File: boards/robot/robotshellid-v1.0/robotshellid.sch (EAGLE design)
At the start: 38 parts, among them IC1 PCA9848PWJ, U2 TSL25721FN, U3 TSL25721FN, U4 TSL25721FN, U5 TSL25721FN, U6 MIC5501-3.0YM5-TR

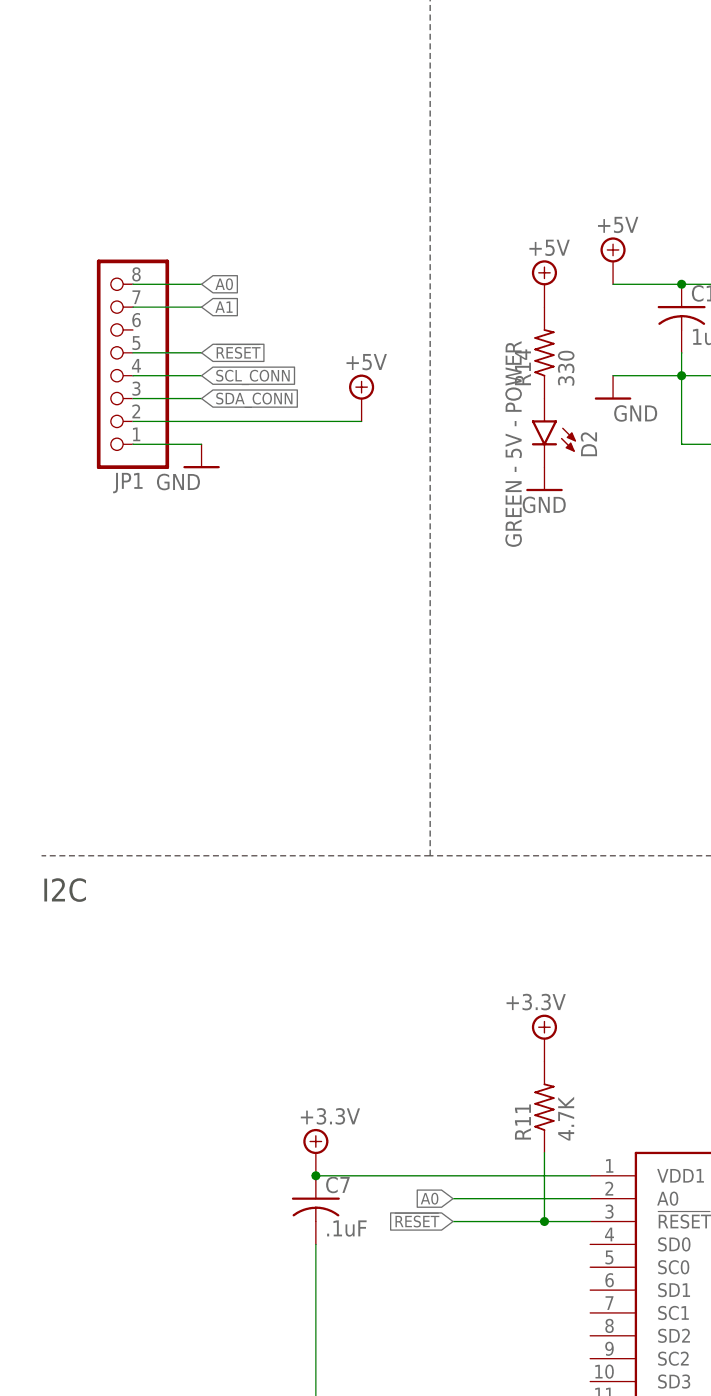
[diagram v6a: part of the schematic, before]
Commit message: Changed connector out for ffc connector
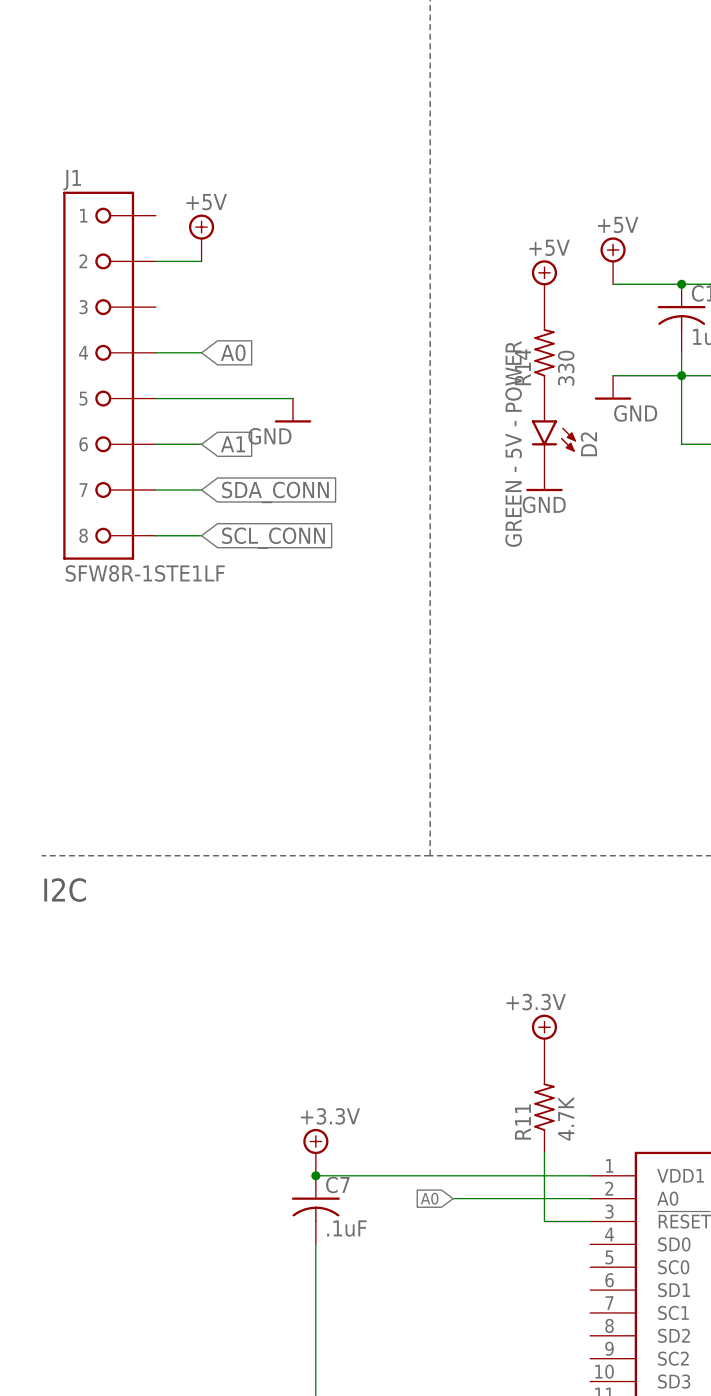
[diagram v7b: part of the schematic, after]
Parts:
- removed JP1: (no value), RoboJackets-Connectors:PINHD-1X8
- added J1: SFW8R-1STE1LF, RoboJackets-Connectors:SFW8R-1STE1LF
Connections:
- net !RESET: no longer JP1.5
- net +5V: now also J1.2; no longer JP1.2
- net A0: now also J1.4; no longer JP1.8
- net A1: now also J1.6; no longer JP1.7
- net GND: now also J1.5; no longer JP1.1
- net SCL_CONN: now also J1.8; no longer JP1.4
- net SDA_CONN: now also J1.7; no longer JP1.3
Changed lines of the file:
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@@
 <part name="SUPPLY9" library="RoboJackets-Supplies" deviceset="+3.3V" device=""/>
 <part name="SUPPLY10" library="RoboJackets-Supplies" deviceset="+3.3V" device=""/>
-<part name="JP1" library="RoboJackets-Connectors" deviceset="PINHD-1X8" device="" package3d_urn="urn:adsk.eagle:package:22409/2"/>
 <part name="R11" library="rcl" library_urn="urn:adsk.eagle:library:334" deviceset="R-US_" device="R0603" package3d_urn="urn:adsk.eagle:package:23555/3" value="4.7K"/>
 <part name="SUPPLY11" library="RoboJackets-Supplies" deviceset="+3.3V" device=""/>
@@
 <part name="SUPPLY16" library="RoboJackets-Supplies" deviceset="GND" device=""/>
 <part name="SUPPLY17" library="RoboJackets-Supplies" deviceset="GND" device=""/>
-<part name="SUPPLY18" library="RoboJackets-Supplies" deviceset="+5V" device=""/>
 <part name="SUPPLY19" library="RoboJackets-Supplies" deviceset="+3.3V" device=""/>
 <part name="SUPPLY20" library="RoboJackets-Supplies" deviceset="+3.3V" device=""/>
@@
 <part name="C7" library="rcl" library_urn="urn:adsk.eagle:library:334" deviceset="C-US" device="C0603" package3d_urn="urn:adsk.eagle:package:23616/2" value=".1uF"/>
 <part name="SUPPLY39" library="RoboJackets-Supplies" deviceset="+3.3V" device=""/>
+<part name="J1" library="RoboJackets-Connectors" deviceset="SFW8R-1STE1LF" device=""/>
+<part name="SUPPLY18" library="supply2" library_urn="urn:adsk.eagle:library:372" deviceset="+5V" device=""/>
 </parts>
 <sheets>
@@
 <attribute name="VALUE" x="94.615" y="130.175" size="1.778" layer="96"/>
 </instance>
-<instance part="JP1" gate="A" x="12.7" y="208.28" smashed="yes" rot="R180">
-<attribute name="NAME" x="16.51" y="194.945" size="1.778" layer="95" rot="R180"/>
-<attribute name="VALUE" x="19.05" y="220.98" size="1.778" layer="96" rot="R180"/>
-</instance>
 <instance part="R11" gate="G$1" x="60.96" y="124.46" smashed="yes" rot="R90">
 <attribute name="NAME" x="59.4614" y="120.65" size="1.778" layer="95" rot="R90"/>
@@
 <attribute name="VALUE" x="56.515" y="135.255" size="1.778" layer="96"/>
 </instance>
-<instance part="SUPPLY12" gate="G$1" x="22.86" y="195.58" smashed="yes">
-<attribute name="VALUE" x="17.78" y="193.04" size="1.778" layer="96"/>
+<instance part="SUPPLY12" gate="G$1" x="33.02" y="200.66" smashed="yes">
+<attribute name="VALUE" x="27.94" y="198.12" size="1.778" layer="96"/>
 </instance>
 <instance part="SUPPLY13" gate="G$1" x="58.42" y="81.28" smashed="yes">
@@
 <instance part="SUPPLY17" gate="G$1" x="213.36" y="96.52" smashed="yes">
 <attribute name="VALUE" x="210.82" y="93.98" size="1.778" layer="96"/>
-</instance>
-<instance part="SUPPLY18" gate="G$1" x="40.64" y="203.2" smashed="yes">
-<attribute name="VALUE" x="38.735" y="206.375" size="1.778" layer="96"/>
 </instance>
 <instance part="SUPPLY19" gate="P" x="129.54" y="119.38" smashed="yes">
@@
 <instance part="SUPPLY39" gate="P" x="35.56" y="119.38" smashed="yes">
 <attribute name="VALUE" x="33.655" y="122.555" size="1.778" layer="96"/>
+</instance>
+<instance part="J1" gate="G$1" x="12.7" y="205.74" smashed="yes">
+<attribute name="NAME" x="7.62" y="228.6" size="1.778" layer="95" font="vector" align="top-left"/>
+<attribute name="VALUE" x="7.62" y="182.88" size="1.778" layer="96" font="vector"/>
+</instance>
+<instance part="SUPPLY18" gate="+5V" x="22.86" y="220.98" smashed="yes">
+<attribute name="VALUE" x="20.955" y="224.155" size="1.778" layer="96"/>
 </instance>
 </instances>
@@
 </segment>
 <segment>
-<pinref part="JP1" gate="A" pin="4"/>
-<wire x1="15.24" y1="205.74" x2="22.86" y2="205.74" width="0.1524" layer="91"/>
-<label x="22.86" y="205.74" size="1.27" layer="95" xref="yes"/>
+<pinref part="J1" gate="G$1" pin="8"/>
+<wire x1="17.78" y1="187.96" x2="22.86" y2="187.96" width="0.1524" layer="91"/>
+<label x="22.86" y="187.96" size="1.778" layer="95" xref="yes"/>
 </segment>
 </net>
@@
 </segment>
 <segment>
-<pinref part="JP1" gate="A" pin="3"/>
-<wire x1="15.24" y1="203.2" x2="22.86" y2="203.2" width="0.1524" layer="91"/>
-<label x="22.86" y="203.2" size="1.27" layer="95" xref="yes"/>
+<pinref part="J1" gate="G$1" pin="7"/>
+<wire x1="17.78" y1="193.04" x2="22.86" y2="193.04" width="0.1524" layer="91"/>
+<label x="22.86" y="193.04" size="1.778" layer="95" xref="yes"/>
 </segment>
 </net>
@@
 </segment>
 <segment>
-<pinref part="JP1" gate="A" pin="8"/>
-<wire x1="15.24" y1="215.9" x2="22.86" y2="215.9" width="0.1524" layer="91"/>
-<label x="22.86" y="215.9" size="1.27" layer="95" xref="yes"/>
+<pinref part="J1" gate="G$1" pin="4"/>
+<wire x1="17.78" y1="208.28" x2="22.86" y2="208.28" width="0.1524" layer="91"/>
+<label x="22.86" y="208.28" size="1.778" layer="95" xref="yes"/>
 </segment>
 </net>
@@
 </segment>
 <segment>
-<pinref part="JP1" gate="A" pin="7"/>
-<wire x1="15.24" y1="213.36" x2="22.86" y2="213.36" width="0.1524" layer="91"/>
-<label x="22.86" y="213.36" size="1.27" layer="95" xref="yes"/>
+<pinref part="J1" gate="G$1" pin="6"/>
+<wire x1="17.78" y1="198.12" x2="22.86" y2="198.12" width="0.1524" layer="91"/>
+<label x="22.86" y="198.12" size="1.778" layer="95" xref="yes"/>
 </segment>
 </net>
 <net name="!RESET" class="0">
 <segment>
-<pinref part="JP1" gate="A" pin="5"/>
-<wire x1="15.24" y1="208.28" x2="22.86" y2="208.28" width="0.1524" layer="91"/>
-<label x="22.86" y="208.28" size="1.27" layer="95" xref="yes"/>
-</segment>
-<segment>
 <pinref part="IC1" gate="G$1" pin="!RESET"/>
-<label x="50.8" y="111.76" size="1.27" layer="95" rot="R180" xref="yes"/>
 <pinref part="R11" gate="G$1" pin="1"/>
-<wire x1="50.8" y1="111.76" x2="60.96" y2="111.76" width="0.1524" layer="91"/>
 <wire x1="60.96" y1="111.76" x2="66.04" y2="111.76" width="0.1524" layer="91"/>
 <wire x1="60.96" y1="119.38" x2="60.96" y2="111.76" width="0.1524" layer="91"/>
-<junction x="60.96" y="111.76"/>
 </segment>
 </net>
 <net name="GND" class="0">
-<segment>
-<pinref part="JP1" gate="A" pin="1"/>
-<wire x1="15.24" y1="198.12" x2="22.86" y2="198.12" width="0.1524" layer="91"/>
-<pinref part="SUPPLY12" gate="G$1" pin="GND"/>
-</segment>
 <segment>
 <pinref part="U6" gate="G$1" pin="GND"/>
@@
 <junction x="213.36" y="218.44"/>
 </segment>
+<segment>
+<pinref part="J1" gate="G$1" pin="5"/>
+<pinref part="SUPPLY12" gate="G$1" pin="GND"/>
+<wire x1="17.78" y1="203.2" x2="33.02" y2="203.2" width="0.1524" layer="91"/>
+</segment>
 </net>
 <net name="+5V" class="0">
@@
 </segment>
 <segment>
-<pinref part="JP1" gate="A" pin="2"/>
-<pinref part="SUPPLY18" gate="G$1" pin="+5V"/>
-<wire x1="15.24" y1="200.66" x2="40.64" y2="200.66" width="0.1524" layer="91"/>
-</segment>
-</net>
+<pinref part="J1" gate="G$1" pin="2"/>
+<wire x1="17.78" y1="218.44" x2="22.86" y2="218.44" width="0.1524" layer="91"/>
+<pinref part="SUPPLY18" gate="+5V" pin="+5V"/>
+</segment>
+</net>

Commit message: dr changes
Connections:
- removed net A0: IC1.A0, J1.4
- removed net A1: IC1.A1, J1.6
- new net !RST!-I2C: IC1.A1, J1.4
- new net INT-I2C: IC1.A0, J1.5
- net +5V: now also J1.1; no longer J1.2
- net GND: now also J1.7; no longer J1.5
- net SCL_CONN: now also J1.2; no longer J1.8
- net SDA_CONN: now also J1.3; no longer J1.7
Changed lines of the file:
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@@
 <attribute name="VALUE" x="56.515" y="135.255" size="1.778" layer="96"/>
 </instance>
-<instance part="SUPPLY12" gate="G$1" x="33.02" y="200.66" smashed="yes">
-<attribute name="VALUE" x="27.94" y="198.12" size="1.778" layer="96"/>
+<instance part="SUPPLY12" gate="G$1" x="22.86" y="190.5" smashed="yes">
+<attribute name="VALUE" x="17.78" y="187.96" size="1.778" layer="96"/>
 </instance>
 <instance part="SUPPLY13" gate="G$1" x="58.42" y="81.28" smashed="yes">
@@
 <attribute name="VALUE" x="7.62" y="182.88" size="1.778" layer="96" font="vector"/>
 </instance>
-<instance part="SUPPLY18" gate="+5V" x="22.86" y="220.98" smashed="yes">
-<attribute name="VALUE" x="20.955" y="224.155" size="1.778" layer="96"/>
+<instance part="SUPPLY18" gate="+5V" x="22.86" y="226.06" smashed="yes">
+<attribute name="VALUE" x="20.955" y="229.235" size="1.778" layer="96"/>
 </instance>
 </instances>
@@
 </segment>
 <segment>
-<pinref part="J1" gate="G$1" pin="8"/>
-<wire x1="17.78" y1="187.96" x2="22.86" y2="187.96" width="0.1524" layer="91"/>
-<label x="22.86" y="187.96" size="1.778" layer="95" xref="yes"/>
+<pinref part="J1" gate="G$1" pin="2"/>
+<wire x1="17.78" y1="218.44" x2="22.86" y2="218.44" width="0.1524" layer="91"/>
+<label x="22.86" y="218.44" size="1.27" layer="95" xref="yes"/>
 </segment>
 </net>
@@
 </segment>
 <segment>
-<pinref part="J1" gate="G$1" pin="7"/>
-<wire x1="17.78" y1="193.04" x2="22.86" y2="193.04" width="0.1524" layer="91"/>
-<label x="22.86" y="193.04" size="1.778" layer="95" xref="yes"/>
-</segment>
-</net>
-<net name="A0" class="0">
-<segment>
-<label x="50.8" y="114.3" size="1.27" layer="95" rot="R180" xref="yes"/>
-<wire x1="50.8" y1="114.3" x2="66.04" y2="114.3" width="0.1524" layer="91"/>
-<pinref part="IC1" gate="G$1" pin="A0"/>
-</segment>
-<segment>
-<pinref part="J1" gate="G$1" pin="4"/>
-<wire x1="17.78" y1="208.28" x2="22.86" y2="208.28" width="0.1524" layer="91"/>
-<label x="22.86" y="208.28" size="1.778" layer="95" xref="yes"/>
-</segment>
-</net>
-<net name="A1" class="0">
-<segment>
-<label x="104.14" y="109.22" size="1.27" layer="95" xref="yes"/>
-<wire x1="104.14" y1="109.22" x2="96.52" y2="109.22" width="0.1524" layer="91"/>
-<pinref part="IC1" gate="G$1" pin="A1"/>
-</segment>
-<segment>
-<pinref part="J1" gate="G$1" pin="6"/>
-<wire x1="17.78" y1="198.12" x2="22.86" y2="198.12" width="0.1524" layer="91"/>
-<label x="22.86" y="198.12" size="1.778" layer="95" xref="yes"/>
+<pinref part="J1" gate="G$1" pin="3"/>
+<wire x1="17.78" y1="213.36" x2="22.86" y2="213.36" width="0.1524" layer="91"/>
+<label x="22.86" y="213.36" size="1.27" layer="95" xref="yes"/>
 </segment>
 </net>
@@
 </segment>
 <segment>
-<pinref part="J1" gate="G$1" pin="5"/>
+<pinref part="J1" gate="G$1" pin="7"/>
 <pinref part="SUPPLY12" gate="G$1" pin="GND"/>
-<wire x1="17.78" y1="203.2" x2="33.02" y2="203.2" width="0.1524" layer="91"/>
+<wire x1="17.78" y1="193.04" x2="22.86" y2="193.04" width="0.1524" layer="91"/>
 </segment>
 </net>
@@
 </segment>
 <segment>
-<pinref part="J1" gate="G$1" pin="2"/>
-<wire x1="17.78" y1="218.44" x2="22.86" y2="218.44" width="0.1524" layer="91"/>
+<pinref part="J1" gate="G$1" pin="1"/>
 <pinref part="SUPPLY18" gate="+5V" pin="+5V"/>
+<wire x1="17.78" y1="223.52" x2="22.86" y2="223.52" width="0.1524" layer="91"/>
 </segment>
 </net>
@@
 <segment>
 <junction x="175.26" y="106.68"/>
+</segment>
+</net>
+<net name="!RST!-I2C" class="0">
+<segment>
+<pinref part="J1" gate="G$1" pin="4"/>
+<wire x1="17.78" y1="208.28" x2="22.86" y2="208.28" width="0.1524" layer="91"/>
+<label x="22.86" y="208.28" size="1.27" layer="95" xref="yes"/>
+</segment>
+<segment>
+<label x="104.14" y="109.22" size="1.27" layer="95" xref="yes"/>
+<wire x1="104.14" y1="109.22" x2="96.52" y2="109.22" width="0.1524" layer="91"/>
+<pinref part="IC1" gate="G$1" pin="A1"/>
+</segment>
+</net>
+<net name="INT-I2C" class="0">
+<segment>
+<pinref part="J1" gate="G$1" pin="5"/>
+<wire x1="17.78" y1="203.2" x2="22.86" y2="203.2" width="0.1524" layer="91"/>
+<label x="22.86" y="203.2" size="1.27" layer="95" xref="yes"/>
+</segment>
+<segment>
+<label x="50.8" y="114.3" size="1.27" layer="95" rot="R180" xref="yes"/>
+<wire x1="50.8" y1="114.3" x2="66.04" y2="114.3" width="0.1524" layer="91"/>
+<pinref part="IC1" gate="G$1" pin="A0"/>
 </segment>
 </net>
@@
 </sheet>
 </sheets>
+<errors>
+</errors>
 </schematic>
 </drawing>
